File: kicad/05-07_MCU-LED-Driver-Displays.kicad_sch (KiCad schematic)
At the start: 66 parts, among them J4 Conn_01x03_Pin, J5 Conn_01x03_Pin, J6 Conn_01x02_Pin, J7 Conn_02x05_Counter_Clockwise, Q4 AO3400A, Q5 AO3400A, SW1 USER_A, SW2 USER_B_PWR, SW3 RESET, SW4 BOOTSEL, U5 W25Q128JVS, U6 RP2040, U7 PCF8523T, Y1 ABM8-272-T3, Y2 ABS07AIG-32.768KHZ-7-T

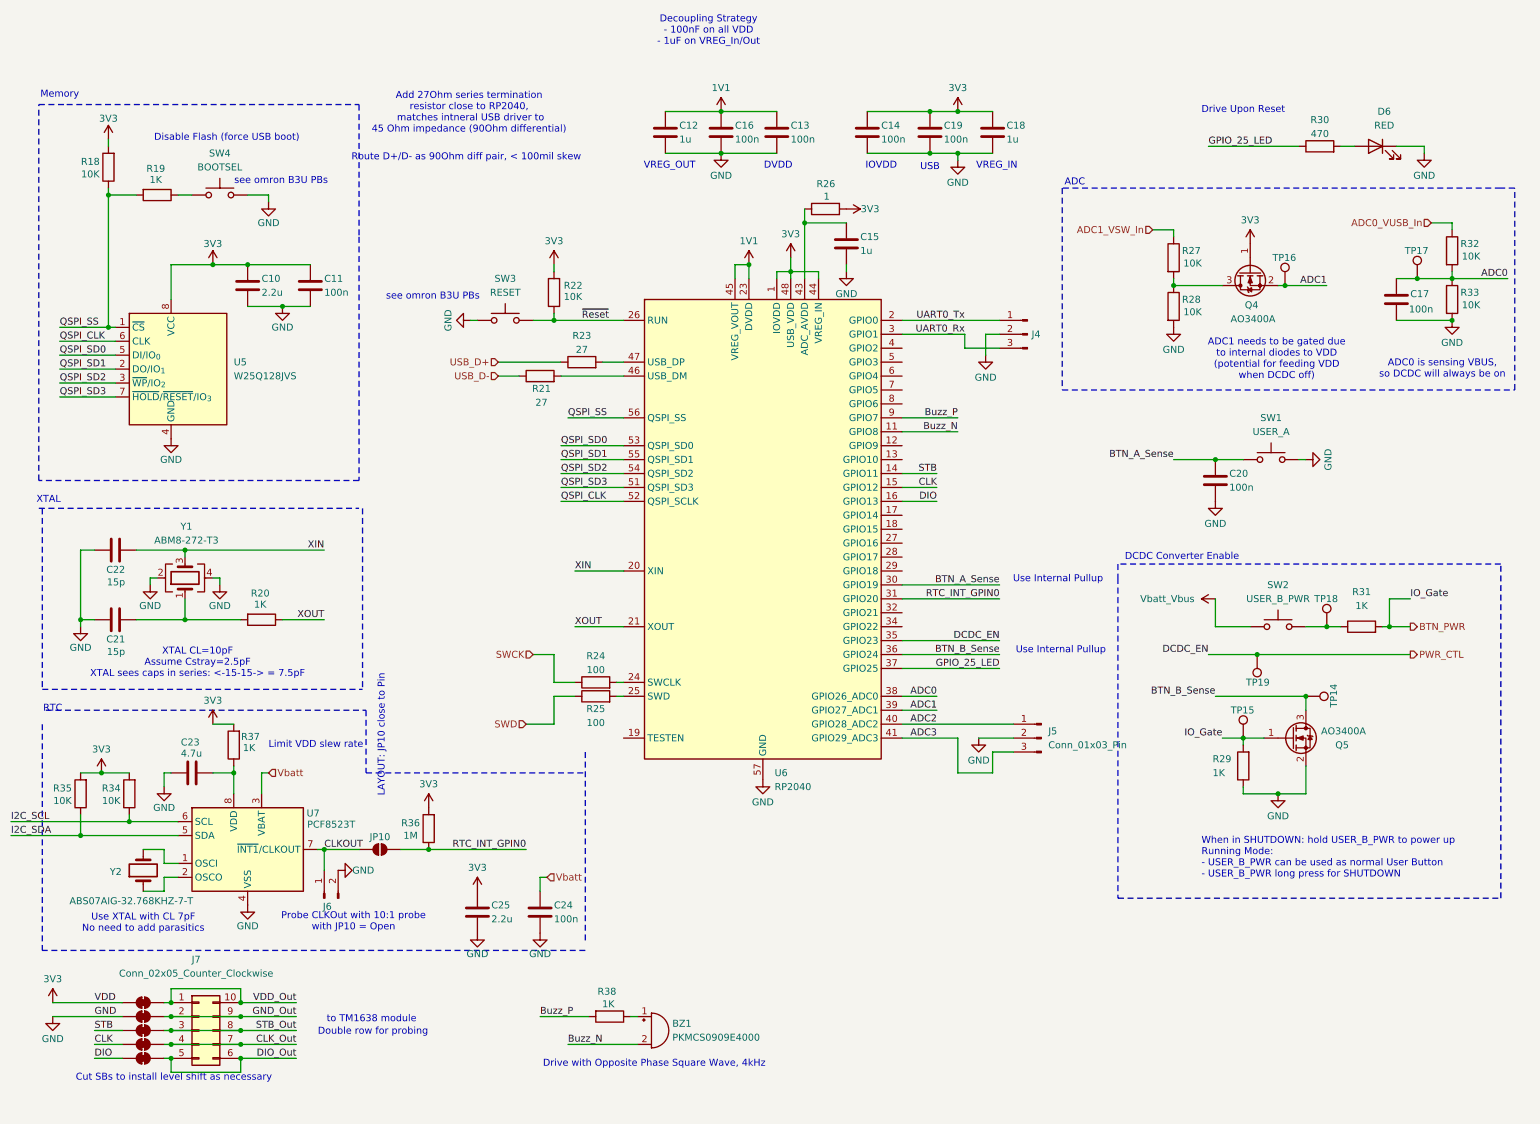
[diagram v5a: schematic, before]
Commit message: DR  ✅ SYS-01-Power-Mux
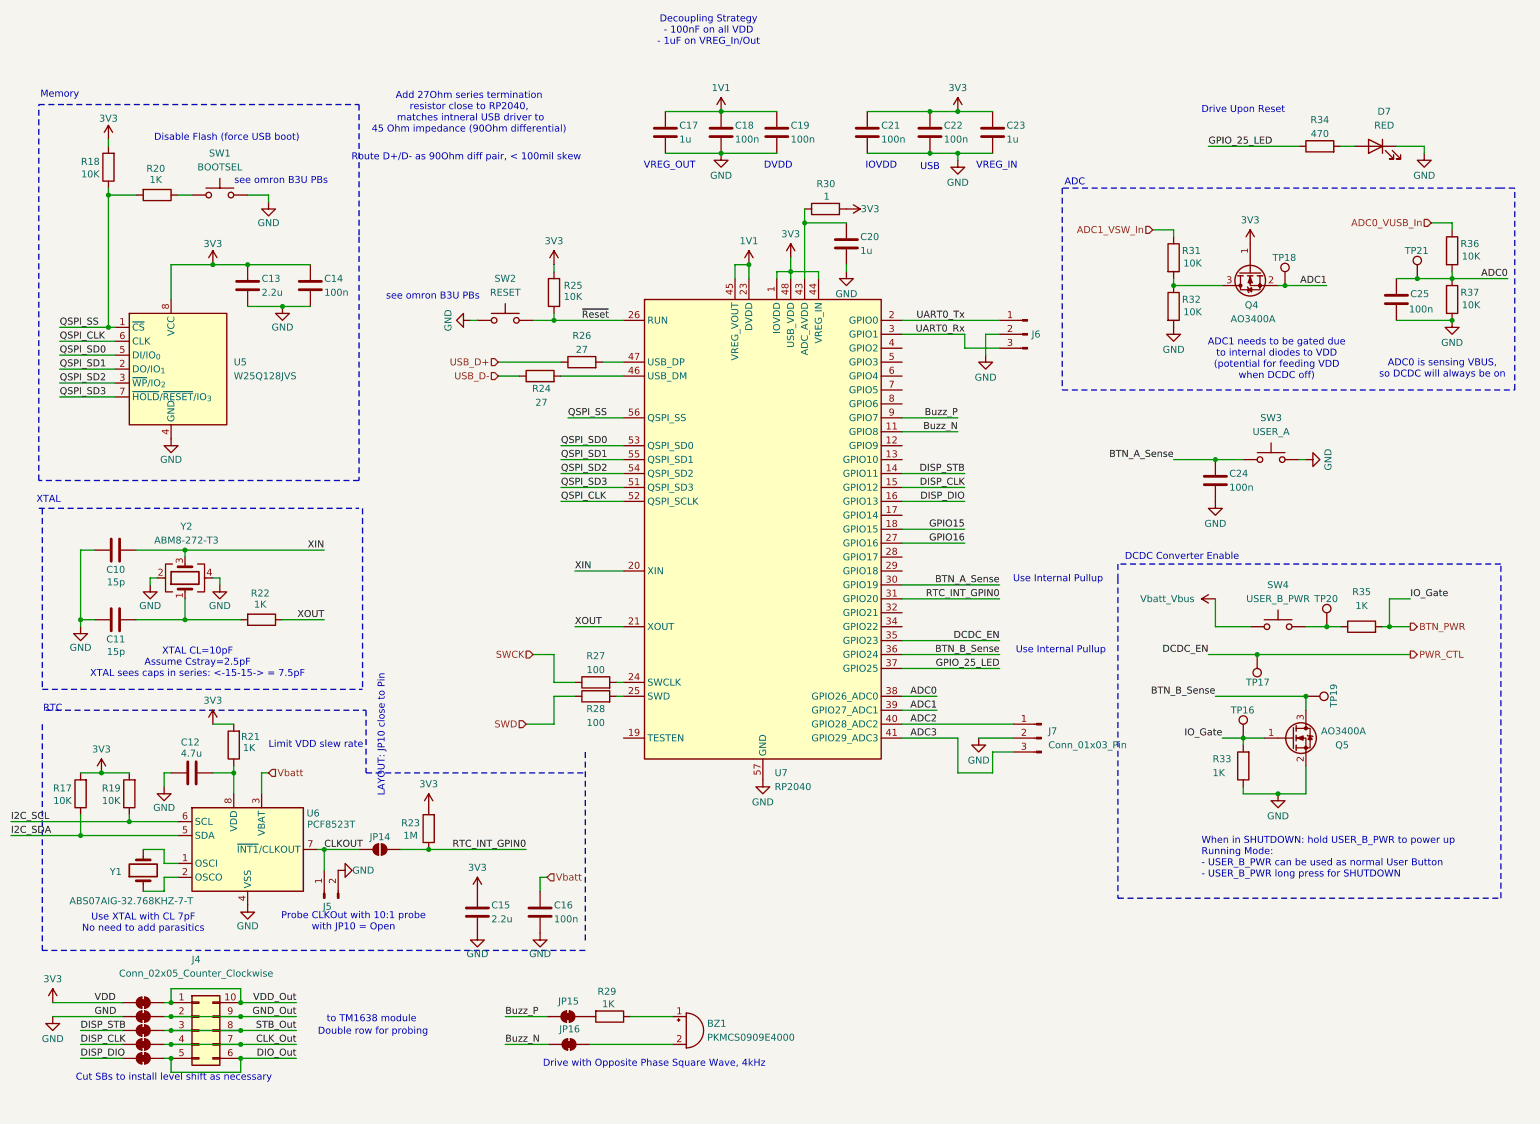
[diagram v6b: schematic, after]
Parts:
- added JP15, JP16: SolderJumper_2_Bridged, Jumper:SolderJumper-2_P1.3mm_Bridged_RoundedPad1.0x1.5mm, symbol Jumper:SolderJumper_2_Bridged
- D7: renamed from D6; footprint (none) -> LED_SMD:LED_0805_2012Metric
- JP10: renamed from JP6; footprint (none) -> Jumper:SolderJumper-2_P1.3mm_Bridged_RoundedPad1.0x1.5mm
- JP11: renamed from JP7; footprint (none) -> Jumper:SolderJumper-2_P1.3mm_Bridged_RoundedPad1.0x1.5mm
- JP12: renamed from JP8; footprint (none) -> Jumper:SolderJumper-2_P1.3mm_Bridged_RoundedPad1.0x1.5mm
- JP13: renamed from JP9; footprint (none) -> Jumper:SolderJumper-2_P1.3mm_Bridged_RoundedPad1.0x1.5mm
- JP14: renamed from JP10; footprint (none) -> Jumper:SolderJumper-2_P1.3mm_Open_RoundedPad1.0x1.5mm
- JP9: renamed from JP5; footprint (none) -> Jumper:SolderJumper-2_P1.3mm_Bridged_RoundedPad1.0x1.5mm
- R17: renamed from R35; footprint (none) -> Resistor_SMD:R_0805_2012Metric_Pad1.20x1.40mm_HandSolder
- R18: footprint (none) -> Resistor_SMD:R_0805_2012Metric_Pad1.20x1.40mm_HandSolder
- R19: renamed from R34; footprint (none) -> Resistor_SMD:R_0805_2012Metric_Pad1.20x1.40mm_HandSolder
- R20: renamed from R19; footprint (none) -> Resistor_SMD:R_0805_2012Metric_Pad1.20x1.40mm_HandSolder
- R21: renamed from R37; footprint (none) -> Resistor_SMD:R_0805_2012Metric_Pad1.20x1.40mm_HandSolder
- R22: renamed from R20; footprint (none) -> Resistor_SMD:R_0805_2012Metric_Pad1.20x1.40mm_HandSolder
- R23: renamed from R36; footprint (none) -> Resistor_SMD:R_0805_2012Metric_Pad1.20x1.40mm_HandSolder
- R24: renamed from R21; footprint (none) -> Resistor_SMD:R_0805_2012Metric_Pad1.20x1.40mm_HandSolder
- R25: renamed from R22; footprint (none) -> Resistor_SMD:R_0805_2012Metric_Pad1.20x1.40mm_HandSolder
- R26: renamed from R23; footprint (none) -> Resistor_SMD:R_0805_2012Metric_Pad1.20x1.40mm_HandSolder
- R27: renamed from R24; footprint (none) -> Resistor_SMD:R_0805_2012Metric_Pad1.20x1.40mm_HandSolder
- R28: renamed from R25; footprint (none) -> Resistor_SMD:R_0805_2012Metric_Pad1.20x1.40mm_HandSolder
- R29: renamed from R38; footprint (none) -> Resistor_SMD:R_0805_2012Metric_Pad1.20x1.40mm_HandSolder
- R30: renamed from R26; footprint (none) -> Resistor_SMD:R_0805_2012Metric_Pad1.20x1.40mm_HandSolder
- R31: renamed from R27; footprint (none) -> Resistor_SMD:R_0805_2012Metric_Pad1.20x1.40mm_HandSolder
- R32: renamed from R28; footprint (none) -> Resistor_SMD:R_0805_2012Metric_Pad1.20x1.40mm_HandSolder
- R33: renamed from R29; footprint (none) -> Resistor_SMD:R_0805_2012Metric_Pad1.20x1.40mm_HandSolder
- R34: renamed from R30; footprint (none) -> Resistor_SMD:R_0805_2012Metric_Pad1.20x1.40mm_HandSolder
- R35: renamed from R31; footprint (none) -> Resistor_SMD:R_0805_2012Metric_Pad1.20x1.40mm_HandSolder
- R36: renamed from R32; footprint (none) -> Resistor_SMD:R_0805_2012Metric_Pad1.20x1.40mm_HandSolder
- R37: renamed from R33; footprint (none) -> Resistor_SMD:R_0805_2012Metric_Pad1.20x1.40mm_HandSolder
- TP16: renamed from TP15; footprint (none) -> project footprints:TestPoint_THTPad_D2.0mm_Drill1.0mm
- TP17: renamed from TP19; footprint (none) -> project footprints:TestPoint_THTPad_D2.0mm_Drill1.0mm
- TP18: renamed from TP16; footprint (none) -> project footprints:TestPoint_THTPad_D2.0mm_Drill1.0mm
- TP19: renamed from TP14; footprint (none) -> project footprints:TestPoint_THTPad_D2.0mm_Drill1.0mm
- TP20: renamed from TP18; footprint (none) -> project footprints:TestPoint_THTPad_D2.0mm_Drill1.0mm
- TP21: renamed from TP17; footprint (none) -> project footprints:TestPoint_THTPad_D2.0mm_Drill1.0mm
- renumbered C22 to C10, C21 to C11, C23 to C12, C10 to C13, C11 to C14, C25 to C15, C24 to C16, C12 to C17, C16 to C18, C13 to C19, C15 to C20, C14 to C21, C19 to C22, C18 to C23, C20 to C24, C17 to C25, J7 to J4, J6 to J5, J4 to J6, J5 to J7, SW4 to SW1, SW3 to SW2, SW1 to SW3, SW2 to SW4, U7 to U6, U6 to U7, Y2 to Y1, Y1 to Y2
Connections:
- net Buzz_N: now also JP16.2 (B); no longer BZ1.2 (-)
- net Buzz_P: now also JP15.2 (B); no longer R29.2
- net GPIO15: now reaches U7.18 (GPIO15)
- net GPIO16: now reaches U7.27 (GPIO16)
- net CLK renamed DISP_CLK
- net DIO renamed DISP_DIO
- net STB renamed DISP_STB
- new net: BZ1.2 (-), JP16.1 (A)
- new net: JP15.1 (A), R29.2
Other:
- moved on the sheet: BZ1

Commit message: DR SYS-02-DCDC ✅
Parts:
- JP10: renamed from JP9; MPN (none) -> (Embedded)
- JP11: renamed from JP10; MPN (none) -> (Embedded)
- JP12: renamed from JP11; MPN (none) -> (Embedded)
- JP13: renamed from JP12; MPN (none) -> (Embedded)
- JP14: renamed from JP13; MPN (none) -> (Embedded)
- JP15: renamed from JP14; MPN (none) -> (Embedded)
- JP16: renamed from JP15; MPN (none) -> (Embedded)
- JP17: renamed from JP16; MPN (none) -> (Embedded)
- TP17: renamed from TP16; MPN (none) -> (Embedded)
- TP18: renamed from TP17; MPN (none) -> (Embedded)
- TP19: renamed from TP18; MPN (none) -> (Embedded)
- TP20: renamed from TP19; MPN (none) -> (Embedded)
- TP21: renamed from TP20; MPN (none) -> (Embedded)
- TP22: renamed from TP21; MPN (none) -> (Embedded)
- renumbered D7 to D8, R17 to R18, R18 to R19, R19 to R20, R20 to R21, R21 to R22, R22 to R23, R23 to R24, R24 to R25, R25 to R26, R26 to R27, R27 to R28, R28 to R29, R29 to R30, R30 to R31, R31 to R32, R32 to R33, R33 to R34, R34 to R35, R35 to R36, R36 to R37, R37 to R38

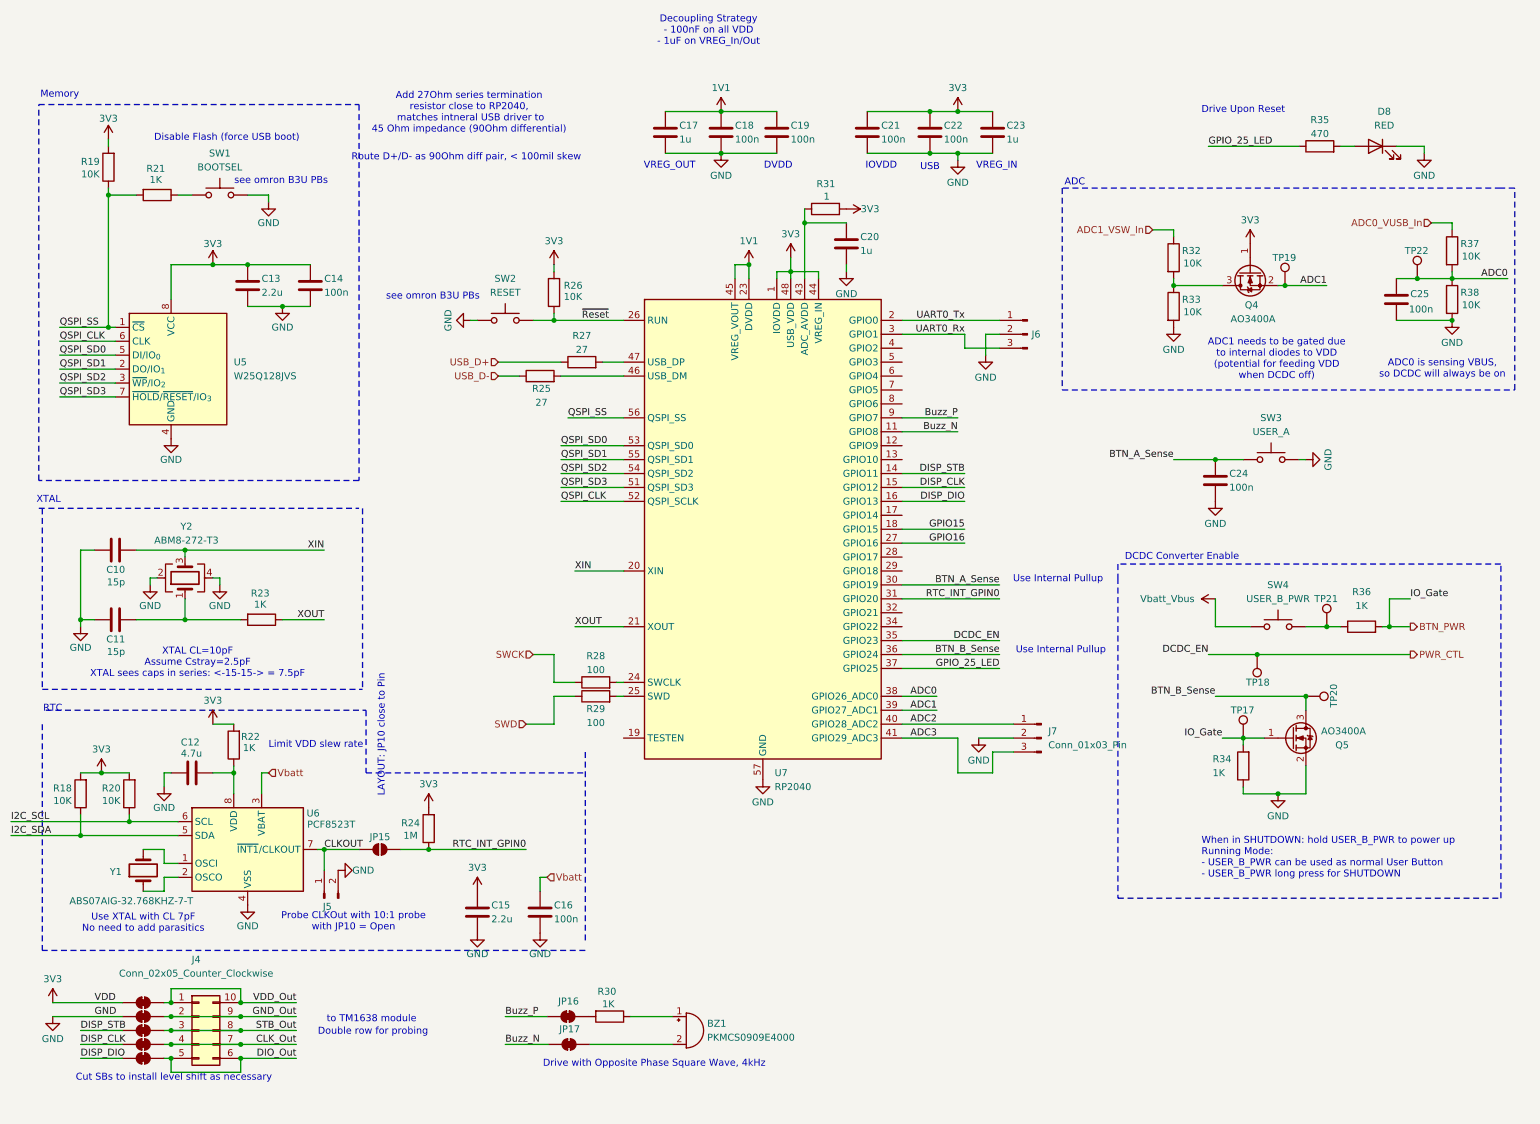
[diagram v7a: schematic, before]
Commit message: charger pcb update
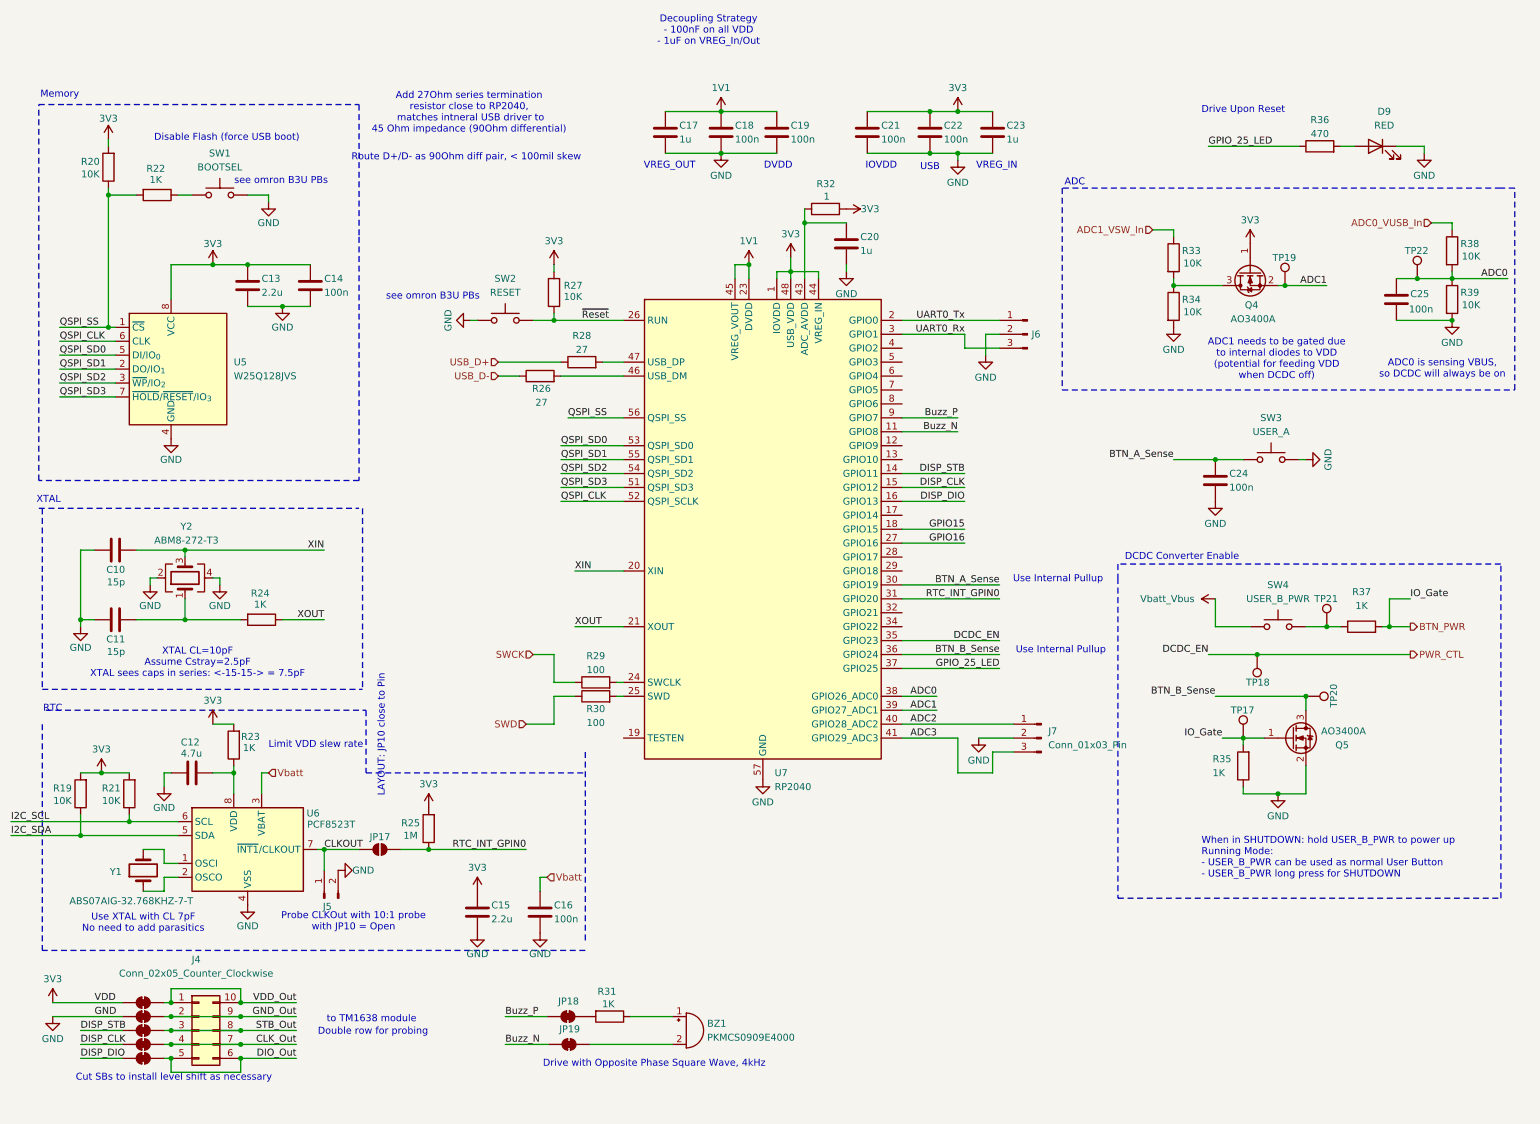
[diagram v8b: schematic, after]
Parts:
- renumbered D8 to D9, JP10 to JP12, JP11 to JP13, JP12 to JP14, JP13 to JP15, JP14 to JP16, JP15 to JP17, JP16 to JP18, JP17 to JP19, R18 to R19, R19 to R20, R20 to R21, R21 to R22, R22 to R23, R23 to R24, R24 to R25, R25 to R26, R26 to R27, R27 to R28, R28 to R29, R29 to R30, R30 to R31, R31 to R32, R32 to R33, R33 to R34, R34 to R35, R35 to R36, R36 to R37, R37 to R38, R38 to R39
